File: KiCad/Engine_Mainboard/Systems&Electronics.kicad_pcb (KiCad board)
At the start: 2 copper layers, 182.4 x 143.2 mm, 56 parts

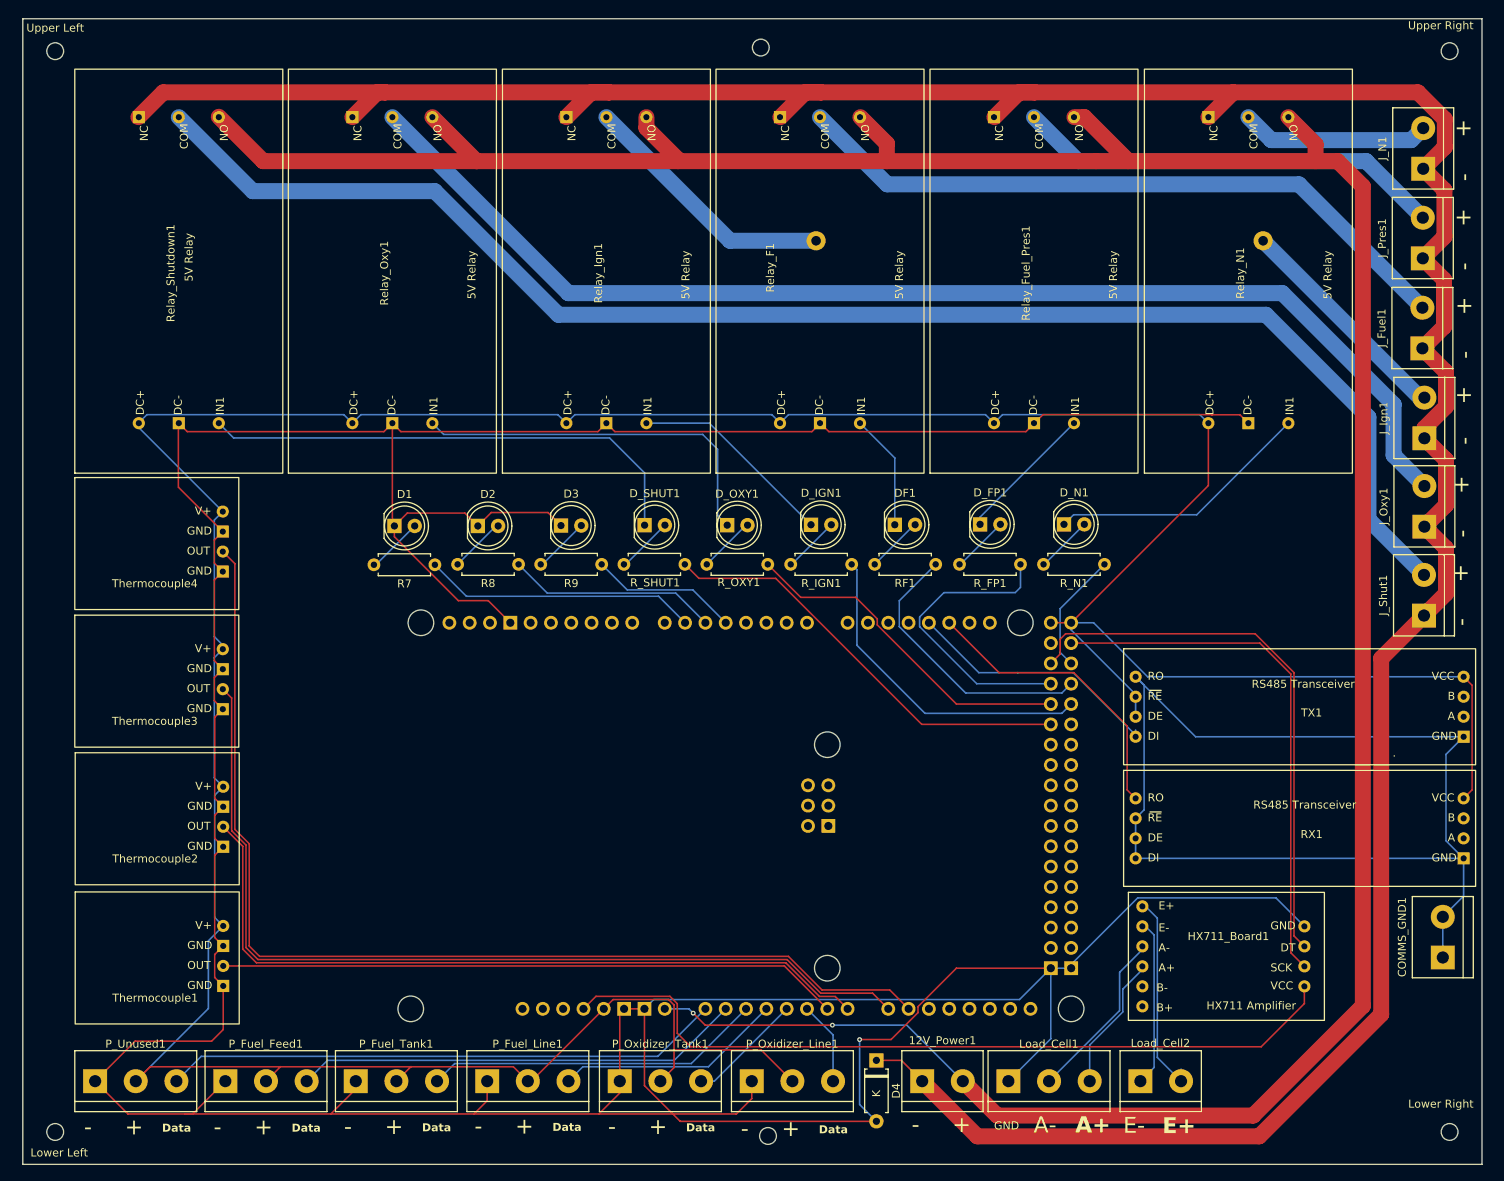
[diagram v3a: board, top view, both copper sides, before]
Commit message: Finishing touches, added redundant power terminals, and reset button.
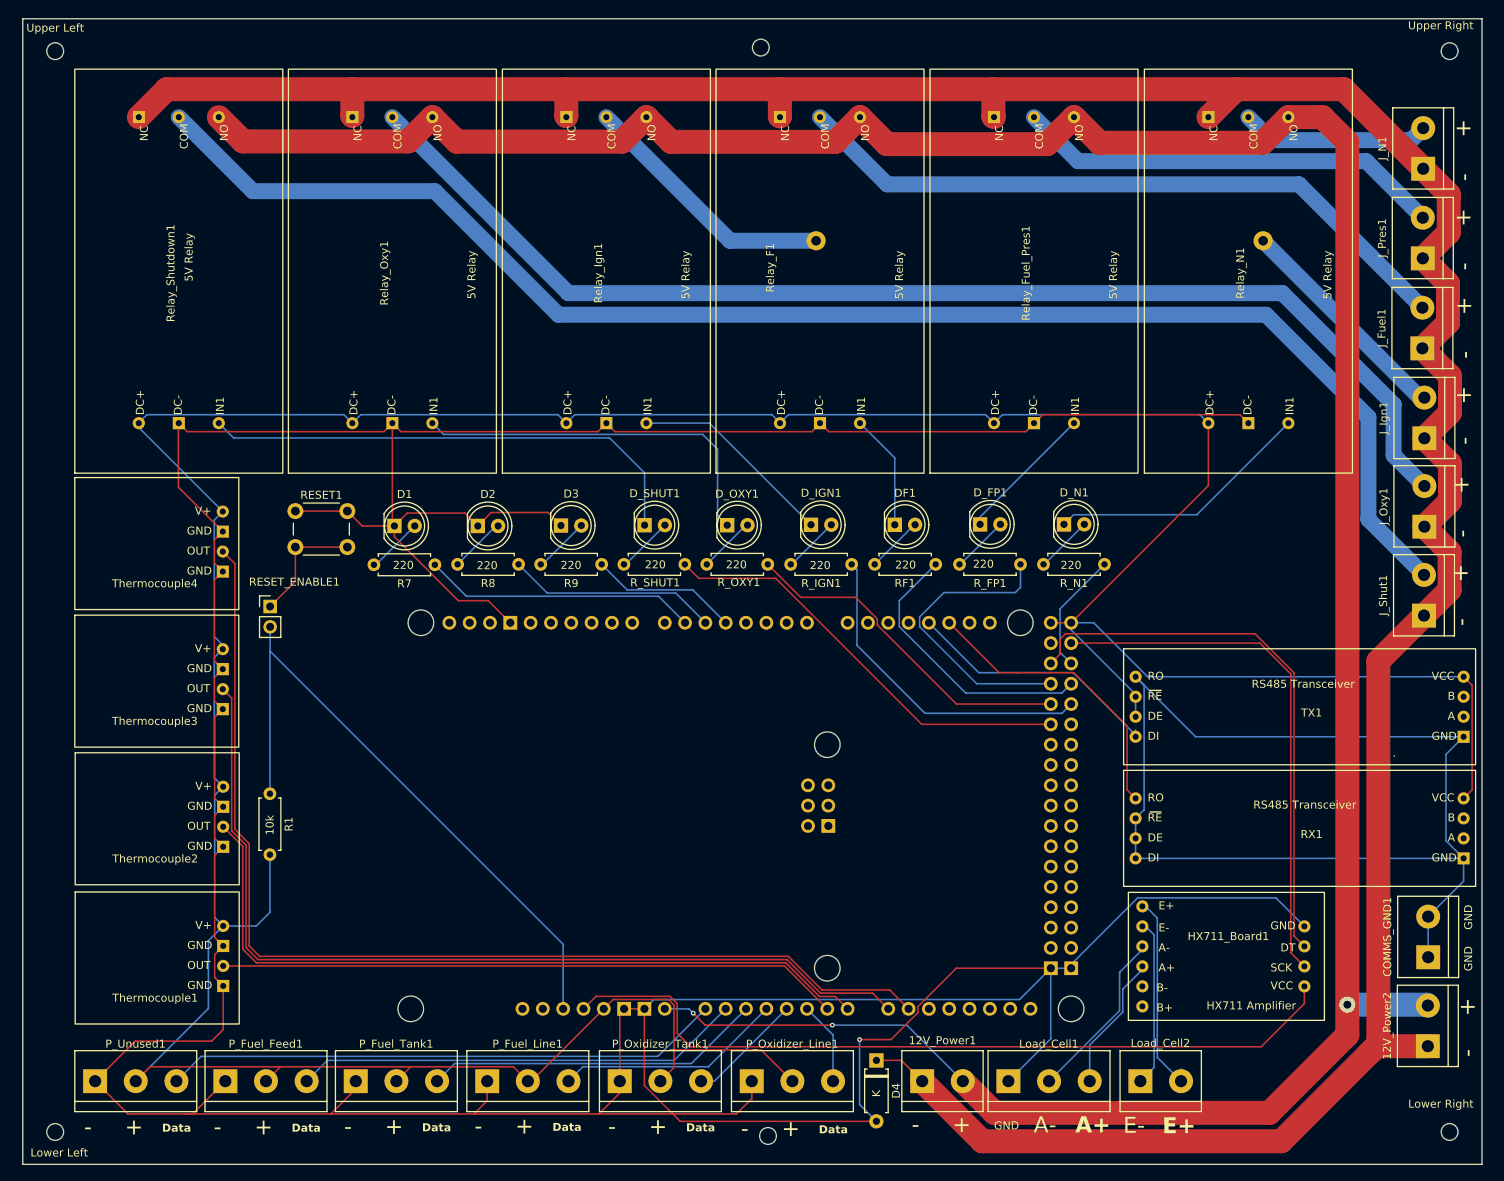
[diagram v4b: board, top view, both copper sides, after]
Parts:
- added 12V_Power2: 12V Aux Power, TerminalBlock:TerminalBlock_bornier-2_P5.08mm, F.Cu at (208.4, 148.6)
- added R1: R, Resistor_THT:R_Axial_DIN0207_L6.3mm_D2.5mm_P7.62mm_Horizontal, F.Cu at (63.7, 117.1)
- added RESET1: Reset, Button_Switch_THT:SW_PUSH_6mm, F.Cu at (66.9, 81.7)
- added RESET_ENABLE1: Jumper_2_Open, Connector_PinHeader_2.54mm:PinHeader_1x02_P2.54mm_Vertical, F.Cu at (63.7, 93.7)
- moved COMMS_GND1 1.83 mm to (208.5, 137.5)
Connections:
- A1 pad RST1: unconnected-(A1-RESET-PadRST1) -> Net-(A1-RESET)
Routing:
- net Net-(A1-RESET): track 0.00 -> 80.8 mm
- net Net-(RESET_ENABLE1-A): track 0.00 -> 15.2 mm
- net Net-(P_Fuel_Feed1-Pin_2): track 454.8 -> 468.6 mm
- net Net-(D1-K): track 603.8 -> 617.5 mm
- net Net-(12V_Power1-Pin_2): track 385.3 -> 371.9 mm, vias 2 -> 3
- net Net-(12V_Power1-Pin_1): track 394.9 -> 389.3 mm
- net Net-(COMMS_GND1-Pin_1): track 139.2 -> 139.9 mm
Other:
- board text added: "10"
- board text added: "10k"
- board text added: "220"

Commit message: minor thermocouple shuffle
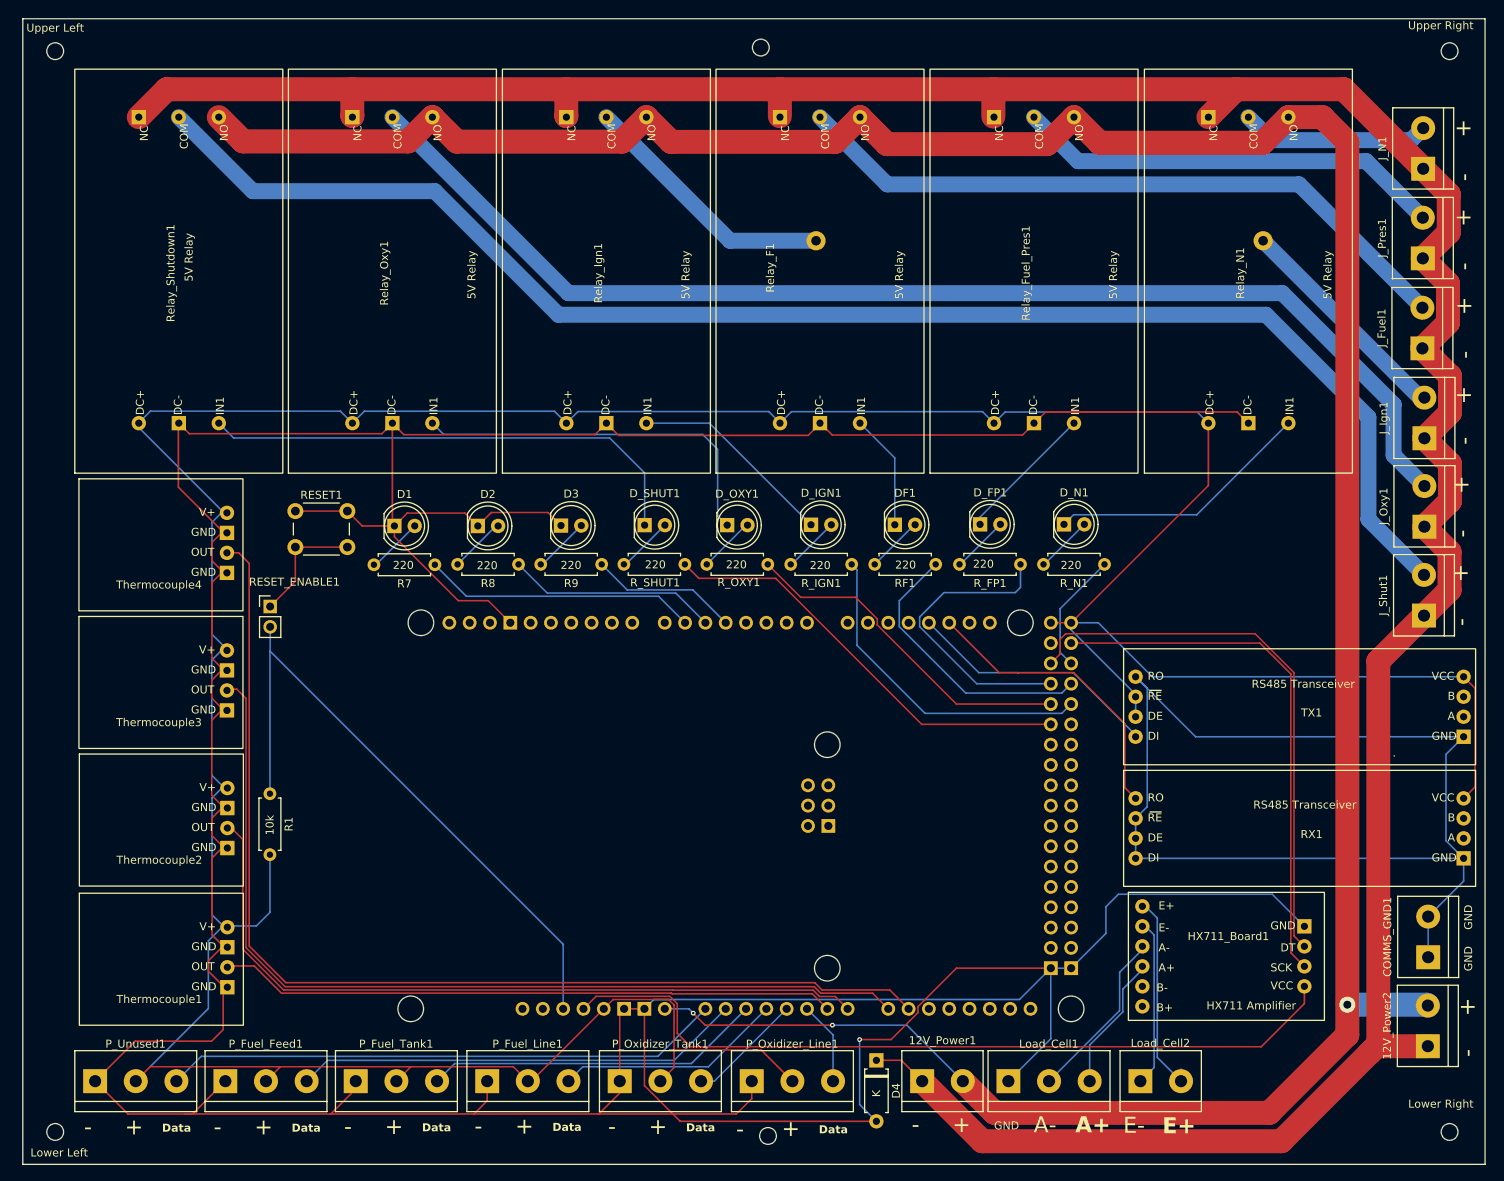
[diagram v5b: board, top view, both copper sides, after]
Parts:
- moved Thermocouple3 0.54 mm to (49.8, 102.2)
- moved Thermocouple4 0.54 mm to (49.8, 85.0)
- moved Thermocouple1 0.54 mm to (49.9, 136.8)
- moved Thermocouple2 0.54 mm to (49.9, 119.4)
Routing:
- net Net-(D1-K): track 617.5 -> 624.0 mm
- net Net-(P_Fuel_Feed1-Pin_2): track 468.6 -> 471.3 mm
- net Net-(A1-PadA8): track 117.0 -> 118.0 mm
- net Net-(A1-PadA7): track 95.0 -> 95.5 mm
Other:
- board size 182.4 x 143.2 mm -> 182.8 x 143.2 mm
- board text removed: "10"

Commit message: trace and hole positioning updates
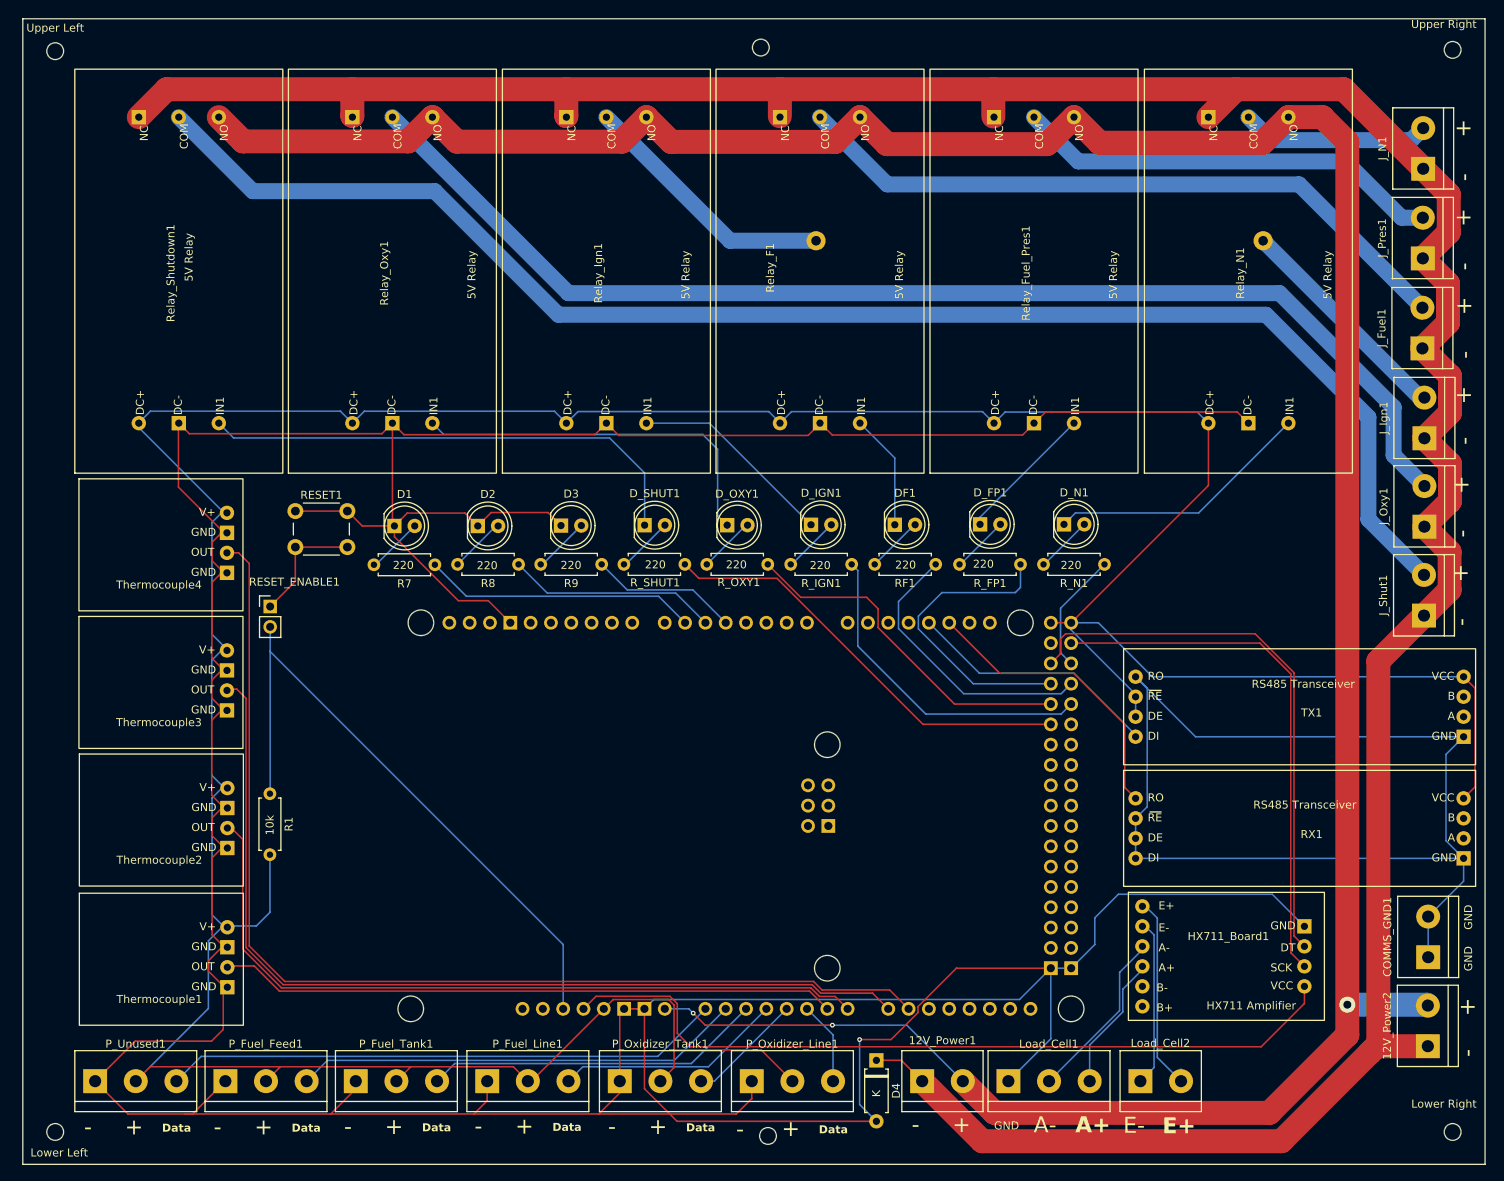
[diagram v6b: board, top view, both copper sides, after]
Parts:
- moved Upper Right 0.41 mm to (211.5, 24.1)
- moved Lower Right 0.38 mm to (211.5, 159.3)
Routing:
- net Net-(A1-PadD28): track 43.1 -> 44.0 mm
- net Net-(A1-PadD26): track 37.6 -> 38.1 mm
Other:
- board text added: "A 30mm clearance between the bottom of the PCB and the mount would be optimal if we need to reprogram the Arduino at any point."
- board text removed: "A 25mm clearance between the bottom of the PCB and the mount would be optimal if we need to reprogram the Arduino at any point."
- board text removed: "The edge holes are all the same size and spacing from the edge."

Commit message: feat(PCB): Final PCB Design
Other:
- board text added: "RPU-1 {dblquote}Reliant{dblquote}"
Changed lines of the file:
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@@
 			(plot_on_all_layers_selection 0x0000000_00000000)
 			(disableapertmacros no)
-			(usegerberextensions no)
-			(usegerberattributes yes)
-			(usegerberadvancedattributes yes)
-			(creategerberjobfile yes)
+			(usegerberextensions yes)
+			(usegerberattributes no)
+			(usegerberadvancedattributes no)
+			(creategerberjobfile no)
 			(dashed_line_dash_ratio 12.000000)
 			(dashed_line_gap_ratio 3.000000)
@@
 			(psa4output no)
 			(plotreference yes)
-			(plotvalue yes)
+			(plotvalue no)
 			(plotfptext yes)
 			(plotinvisibletext no)
 			(sketchpadsonfab no)
-			(subtractmaskfromsilk no)
+			(subtractmaskfromsilk yes)
 			(outputformat 1)
 			(mirror no)
-			(drillshape 1)
+			(drillshape 0)
 			(scaleselection 1)
-			(outputdirectory "")
+			(outputdirectory "C:/Users/coope/Documents/Spaceflight Society/Engine-Mainboard-GBR/")
 		)
 	)
@@
 			(layer "F.CrtYd")
 		)
-		(fp_text user "${REFERENCE}"
-			(at 0 0 0)
-			(layer "F.Fab")
-			(effects
-				(font
-					(size 1 1)
-					(thickness 0.15)
-				)
-			)
-		)
 		(pad "" np_thru_hole circle
 			(at 0 0)
@@
 			(layer "F.CrtYd")
 		)
-		(fp_text user "${REFERENCE}"
-			(at 0 0 0)
-			(layer "F.Fab")
-			(effects
-				(font
-					(size 1 1)
-					(thickness 0.15)
-				)
-			)
-		)
 		(pad "" np_thru_hole circle
 			(at 0 0)
@@
 			(layer "F.CrtYd")
 		)
-		(fp_text user "${REFERENCE}"
-			(at 0 0 0)
-			(layer "F.Fab")
-			(effects
-				(font
-					(size 1 1)
-					(thickness 0.15)
-				)
-			)
-		)
 		(pad "" np_thru_hole circle
 			(at 0 0)
@@
 			(layer "F.CrtYd")
 		)
-		(fp_text user "${REFERENCE}"
-			(at 0 0 0)
-			(layer "F.Fab")
-			(effects
-				(font
-					(size 1 1)
-					(thickness 0.15)
-				)
-			)
-		)
 		(pad "" np_thru_hole circle
 			(at 0 0)
@@
 			(layer "F.CrtYd")
 		)
-		(fp_text user "${REFERENCE}"
-			(at 0 0 0)
-			(layer "F.Fab")
-			(effects
-				(font
-					(size 1 1)
-					(thickness 0.15)
-				)
-			)
-		)
 		(pad "" np_thru_hole circle
 			(at 0 0)
@@
 			(layer "F.CrtYd")
 		)
-		(fp_text user "${REFERENCE}"
-			(at 0 0 0)
-			(layer "F.Fab")
-			(effects
-				(font
-					(size 1 1)
-					(thickness 0.15)
-				)
-			)
-		)
 		(pad "" np_thru_hole circle
 			(at 0 0)
@@
 		)
 	)
+	(gr_text "RPU-1 {dblquote}Reliant{dblquote}"
+		(at 204 67 0)
+		(layer "B.SilkS")
+		(effects
+			(font
+				(size 10 10)
+				(thickness 1)
+				(bold yes)
+			)
+			(justify left bottom mirror)
+		)
+	)
